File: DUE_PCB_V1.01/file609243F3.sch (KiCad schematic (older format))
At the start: 20 parts, among them J28 Motor Left, J29 Cutter Motor, J30 Motor Right, U1 MC33926, U2 MC33926

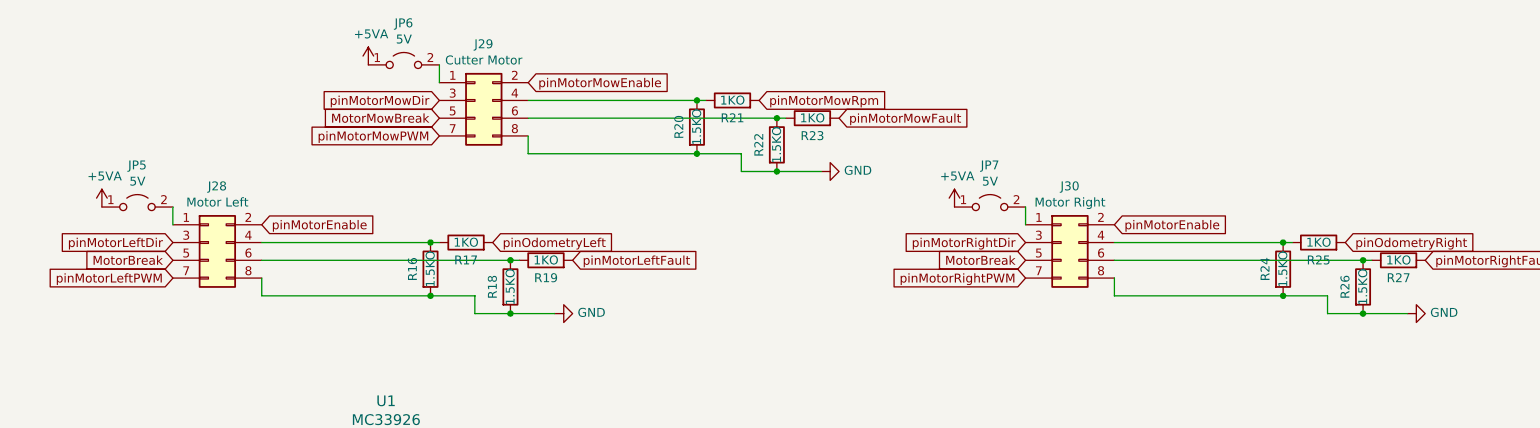
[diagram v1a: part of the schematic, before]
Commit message: Change D6 and D7
Add Description for PIN D6 and D7 to pinFrontMotorLeft and pinFrontMotorRight
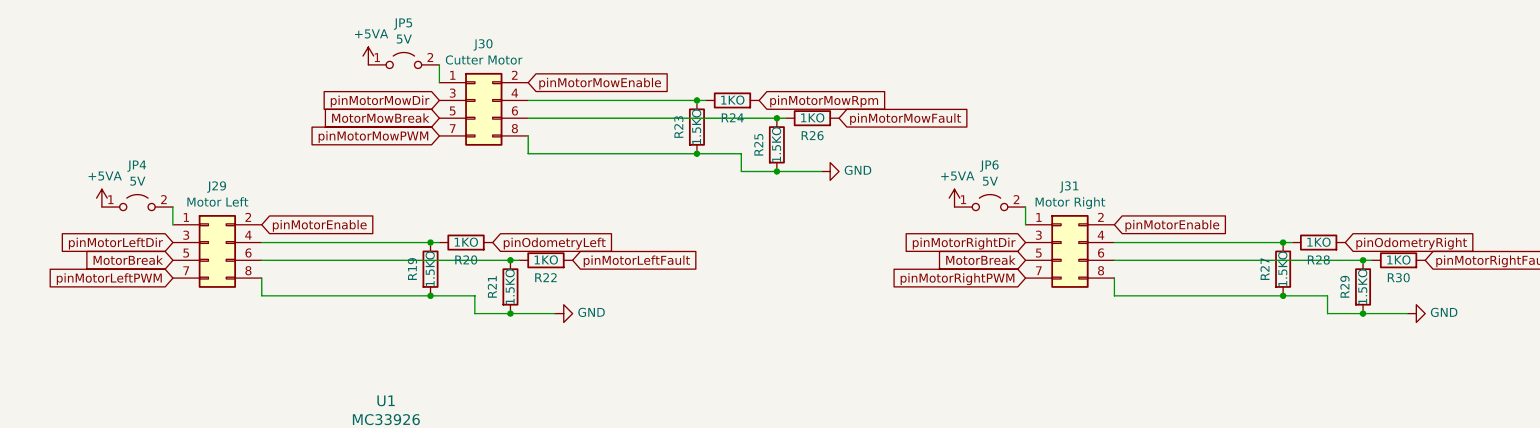
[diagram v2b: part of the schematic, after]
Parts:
- renumbered J28 to J29, J29 to J30, J30 to J31, JP5 to JP4, JP6 to JP5, JP7 to JP6, R16 to R19, R17 to R20, R18 to R21, R19 to R22, R20 to R23, R21 to R24, R22 to R25, R23 to R26, R24 to R27, R25 to R28, R26 to R29, R27 to R30

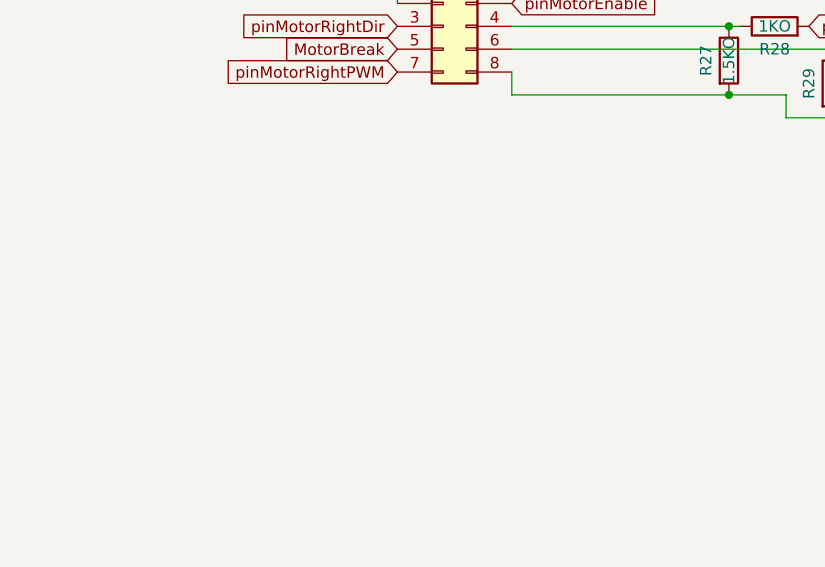
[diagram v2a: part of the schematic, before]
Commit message: Rename Pins
Rename pinFrontMotorLeft to pinMotorLeft2PWM and pinFrontMotorRight to pinMotorRight2PWM
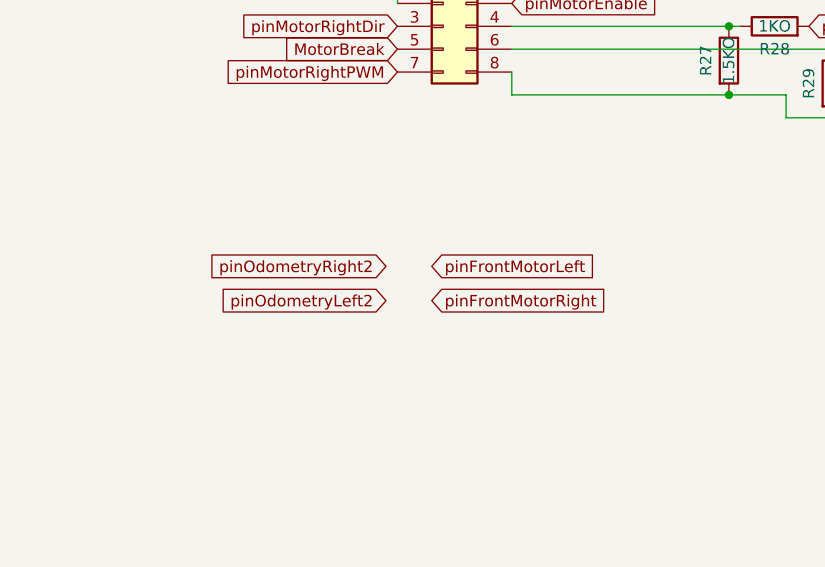
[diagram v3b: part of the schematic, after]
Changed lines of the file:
@@
 	1    0    0    -1
 $EndComp
+Text GLabel 7000 3000 2    50   Input ~ 0
+pinFrontMotorLeft
+Text GLabel 7000 3150 2    50   Input ~ 0
+pinFrontMotorRight
+Text GLabel 6800 3000 0    50   Input ~ 0
+pinOdometryRight2
+Text GLabel 6800 3150 0    50   Input ~ 0
+pinOdometryLeft2
 $EndSCHEMATC

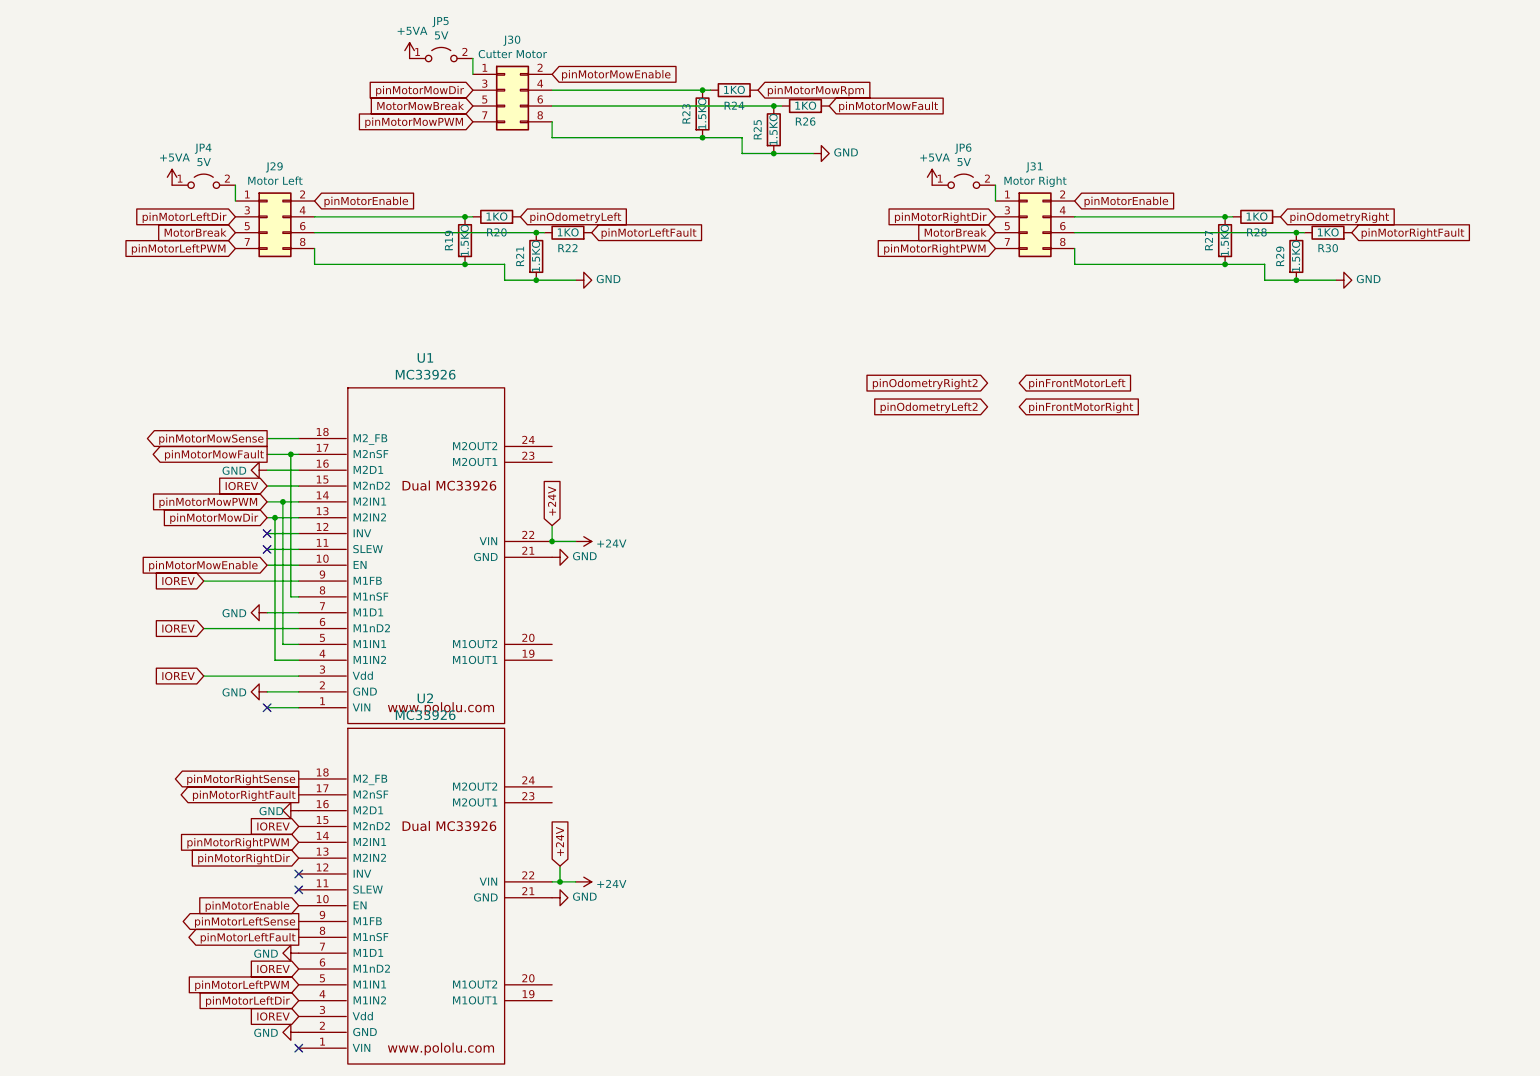
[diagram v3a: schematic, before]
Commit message: Add new Connectors for 4 Mow Motors and Odometrie
Add new Connectors for 4 Mow Motors and Odometrie
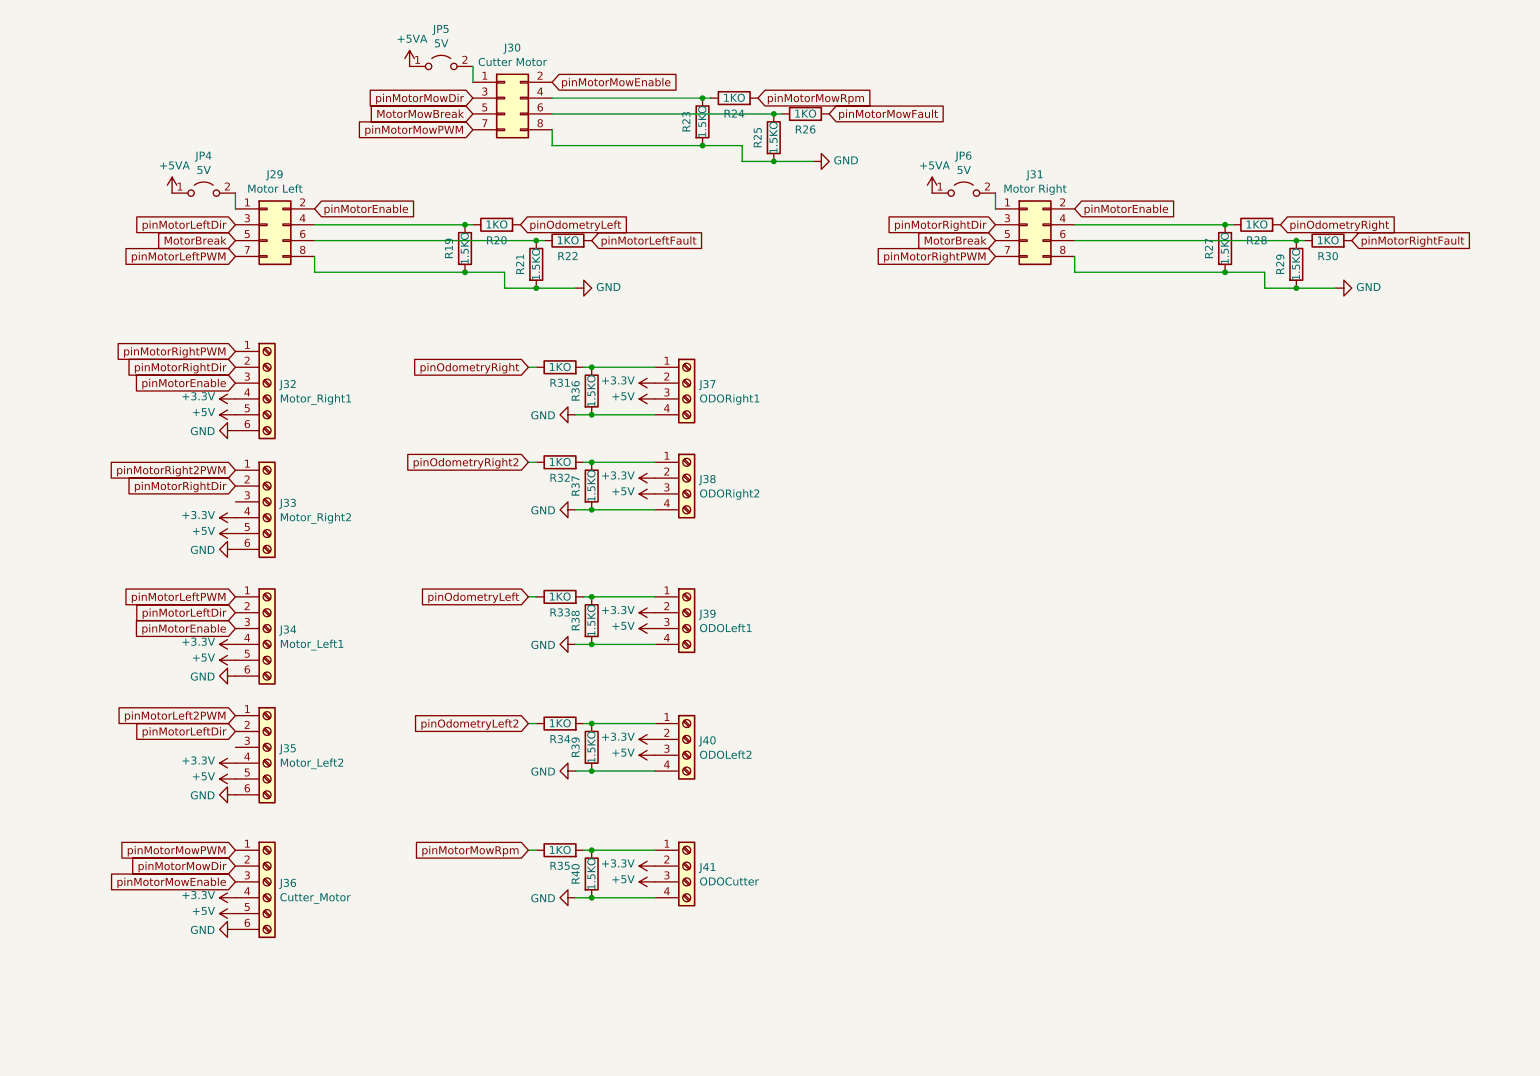
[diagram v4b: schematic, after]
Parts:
- removed U1, U2: MC33926, Zimprich:MC_33926_31polig_mit_Bohrloch_neue_Masse, symbol Lötpad_2,5mm:MC33926
- added J32: Motor_Right1, Connector_PinHeader_2.54mm:PinHeader_1x06_P2.54mm_Vertical, symbol Connector:Screw_Terminal_01x06
- added J33: Motor_Right2, Connector_PinHeader_2.54mm:PinHeader_1x06_P2.54mm_Vertical, symbol Connector:Screw_Terminal_01x06
- added J34: Motor_Left1, Connector_PinHeader_2.54mm:PinHeader_1x06_P2.54mm_Vertical, symbol Connector:Screw_Terminal_01x06
- added J35: Motor_Left2, Connector_PinHeader_2.54mm:PinHeader_1x06_P2.54mm_Vertical, symbol Connector:Screw_Terminal_01x06
- added J36: Cutter_Motor, Connector_PinHeader_2.54mm:PinHeader_1x06_P2.54mm_Vertical, symbol Connector:Screw_Terminal_01x06
- added J37: ODORight1, Connector_PinHeader_2.54mm:PinHeader_1x04_P2.54mm_Vertical, symbol Connector:Screw_Terminal_01x04
- added J38: ODORight2, Connector_PinHeader_2.54mm:PinHeader_1x04_P2.54mm_Vertical, symbol Connector:Screw_Terminal_01x04
- added J39: ODOLeft1, Connector_PinHeader_2.54mm:PinHeader_1x04_P2.54mm_Vertical, symbol Connector:Screw_Terminal_01x04
- added J40: ODOLeft2, Connector_PinHeader_2.54mm:PinHeader_1x04_P2.54mm_Vertical, symbol Connector:Screw_Terminal_01x04
- added J41: ODOCutter, Connector_PinHeader_2.54mm:PinHeader_1x04_P2.54mm_Vertical, symbol Connector:Screw_Terminal_01x04
- added R31, R32, R33, R34, R35: 1KO, Resistor_THT:R_Axial_DIN0207_L6.3mm_D2.5mm_P2.54mm_Vertical, symbol Device:R
- added R36, R37, R38, R39, R40: 1.5KO, Resistor_THT:R_Axial_DIN0207_L6.3mm_D2.5mm_P2.54mm_Vertical, symbol Device:R
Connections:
- net GND: now also J32.6 (Pin_6), J33.6 (Pin_6), J34.6 (Pin_6), J35.6 (Pin_6), J36.6 (Pin_6), J37.4 (Pin_4), J38.4 (Pin_4), J39.4 (Pin_4), J40.4 (Pin_4), J41.4 (Pin_4), R36.2, R37.2, R38.2, R39.2, R40.2
- net pinMotorEnable: now also J32.3 (Pin_3), J34.3 (Pin_3)
- net pinMotorLeftDir: now also J34.2 (Pin_2), J35.2 (Pin_2)
- net pinMotorLeftPWM: now also J34.1 (Pin_1)
- net pinMotorMowDir: now also J36.2 (Pin_2)
- net pinMotorMowEnable: now also J36.3 (Pin_3)
- net pinMotorMowPWM: now also J36.1 (Pin_1)
- net pinMotorMowRpm: now also R35.1
- net pinMotorRightDir: now also J32.2 (Pin_2), J33.2 (Pin_2)
- net pinMotorRightPWM: now also J32.1 (Pin_1)
- net pinOdometryLeft: now also R33.1
- net pinOdometryLeft2: now also R34.1
- net pinOdometryRight: now also R31.1
- net pinOdometryRight2: now also R32.1
- new net: J37.1 (Pin_1), R31.2, R36.1
- new net: J38.1 (Pin_1), R32.2, R37.1
- new net: J39.1 (Pin_1), R33.2, R38.1
- new net: J40.1 (Pin_1), R34.2, R39.1
- new net: J41.1 (Pin_1), R35.2, R40.1
- new net +3V3: J32.4 (Pin_4), J33.4 (Pin_4), J34.4 (Pin_4), J35.4 (Pin_4), J36.4 (Pin_4), J37.2 (Pin_2), J38.2 (Pin_2), J39.2 (Pin_2), J40.2 (Pin_2), J41.2 (Pin_2)
- new net +5V: J32.5 (Pin_5), J33.5 (Pin_5), J34.5 (Pin_5), J35.5 (Pin_5), J36.5 (Pin_5), J37.3 (Pin_3), J38.3 (Pin_3), J39.3 (Pin_3), J40.3 (Pin_3), J41.3 (Pin_3)
- new net pinMotorLeft2PWM: J35.1 (Pin_1)
- new net pinMotorRight2PWM: J33.1 (Pin_1)
- no-connect marks 6 -> 0
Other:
- moved on the sheet: J29, J30, J31, JP4, JP5, JP6, R19, R20, R21, R22, R23, R24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
